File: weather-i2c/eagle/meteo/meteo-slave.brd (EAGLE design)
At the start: 49.5 x 49.5 mm, 38 parts, among them CON1 SPI, IC1 MCP1703CB, J2 RJ12RIGHTANGLE-I2C, J3 RJ12RIGHTANGLE-I2C, U1 ATMEGA328P_TQFP, X1 8MHz, X2 1503_09, X3 1503_09

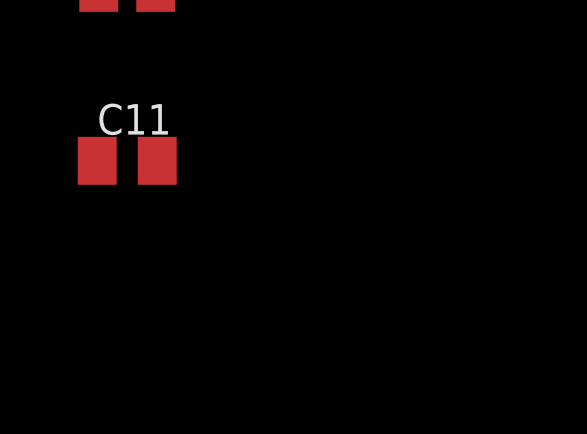
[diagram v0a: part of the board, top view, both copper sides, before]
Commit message: weather-slave: add 4.7k for humidity sensor
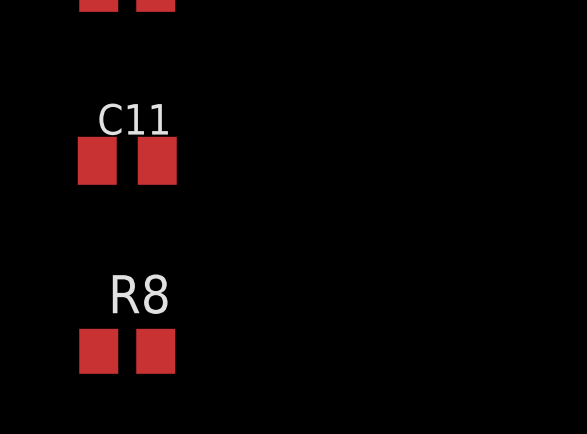
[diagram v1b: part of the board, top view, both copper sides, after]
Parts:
- added R8: 4.7k, resistor:R0805
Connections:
- net D6: now also R8.1
- net D7: now also R8.2
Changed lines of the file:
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@@
 <drawing>
 <settings>
-<setting alwaysvectorfont="no"/>
+<setting alwaysvectorfont="yes"/>
 <setting keepoldvectorfont="yes"/>
 <setting verticaltext="up"/>
@@
 <attribute name="MPN" value="80-C1206C104K5R" x="0.635" y="-20.32" size="1.778" layer="27" display="off"/>
 </element>
+<element name="R8" library="resistor" library_urn="urn:adsk.eagle:library:348" package="R0805" value="4.7k" x="0.635" y="-26.67"/>
 </elements>
 <signals>
@@
 <wire x1="43.37829375" y1="18.32" x2="32.8676" y2="18.32" width="0.4064" layer="1"/>
 <wire x1="44.4714" y1="19.41310625" x2="43.37829375" y2="18.32" width="0.4064" layer="1"/>
+<contactref element="R8" pad="1"/>
+<wire x1="-0.315" y1="-26.67" x2="32.8676" y2="18.32" width="0" layer="19" extent="1-1"/>
 </signal>
 <signal name="D7">
@@
 <wire x1="43.815" y1="19.685" x2="43.815" y2="22.225" width="0.4064" layer="1"/>
 <wire x1="43.815" y1="22.225" x2="45.72" y2="24.13" width="0.4064" layer="1"/>
+<contactref element="R8" pad="2"/>
+<wire x1="1.585" y1="-26.67" x2="32.8676" y2="19.12" width="0" layer="19" extent="1-1"/>
 </signal>
 <signal name="D10">
